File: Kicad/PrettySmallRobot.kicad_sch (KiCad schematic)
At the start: 55 parts, among them J1 TYPE-C-31-M-12, J2 MOTORA_1, J3 MOTORA_2, J4 MOTORB_1, J5 MOTORB_2, J6 BATT+, J7 GND, SW1 SW_Push, SW2 SW_Push, U1 DRV8837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

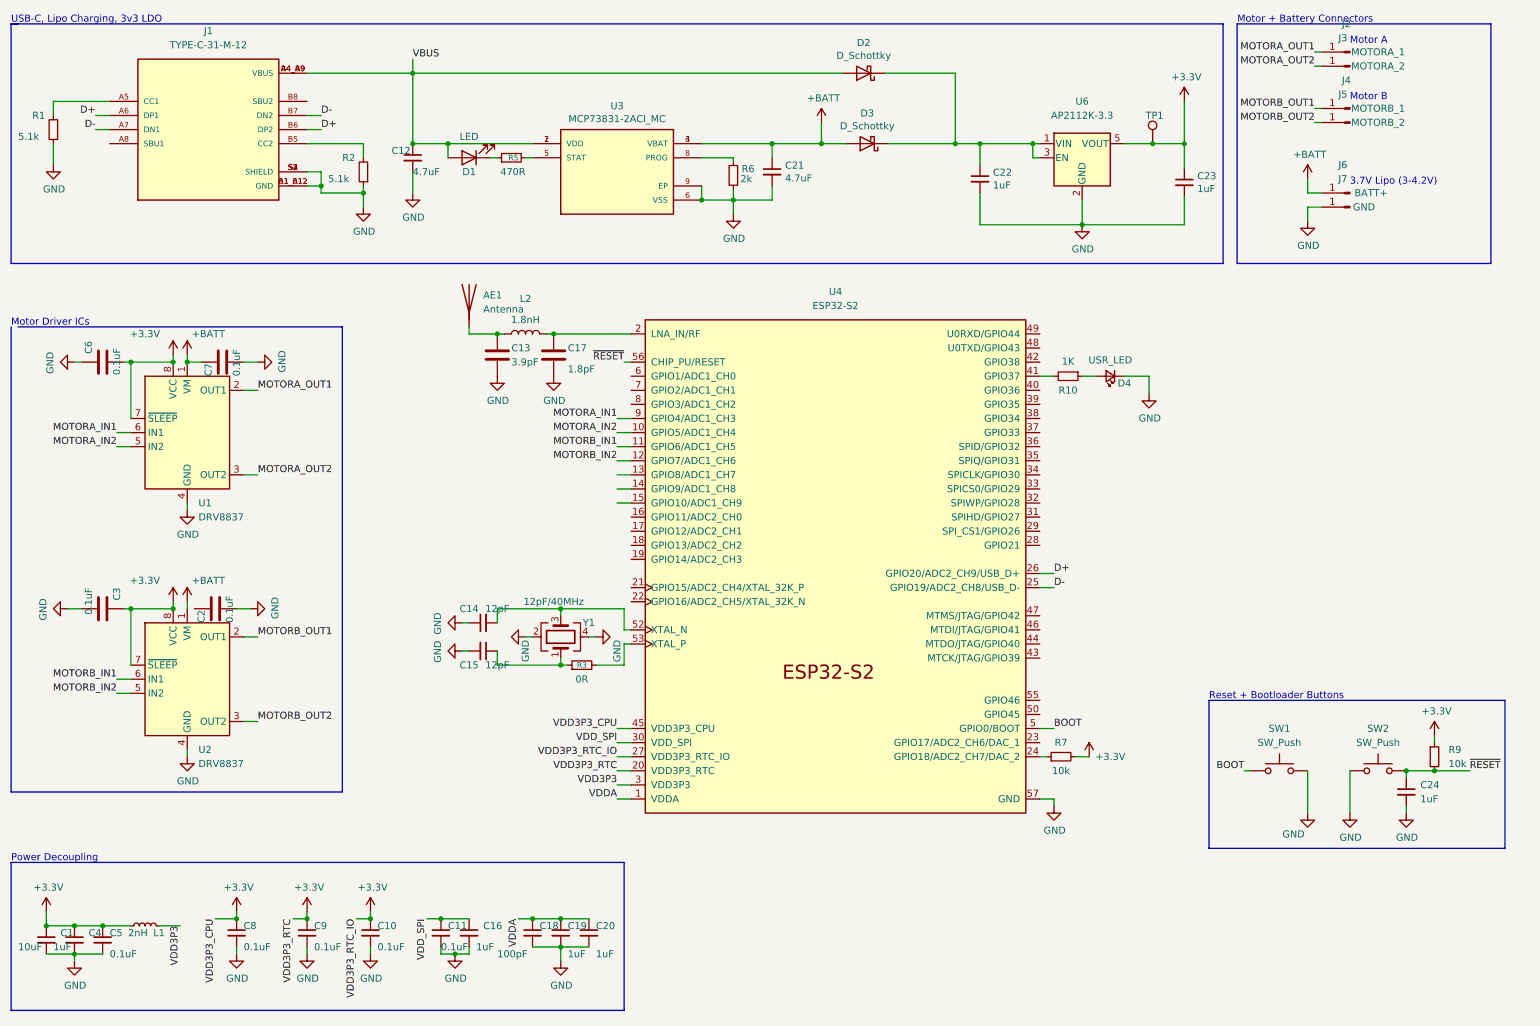
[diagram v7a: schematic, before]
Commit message: fixed drc issues
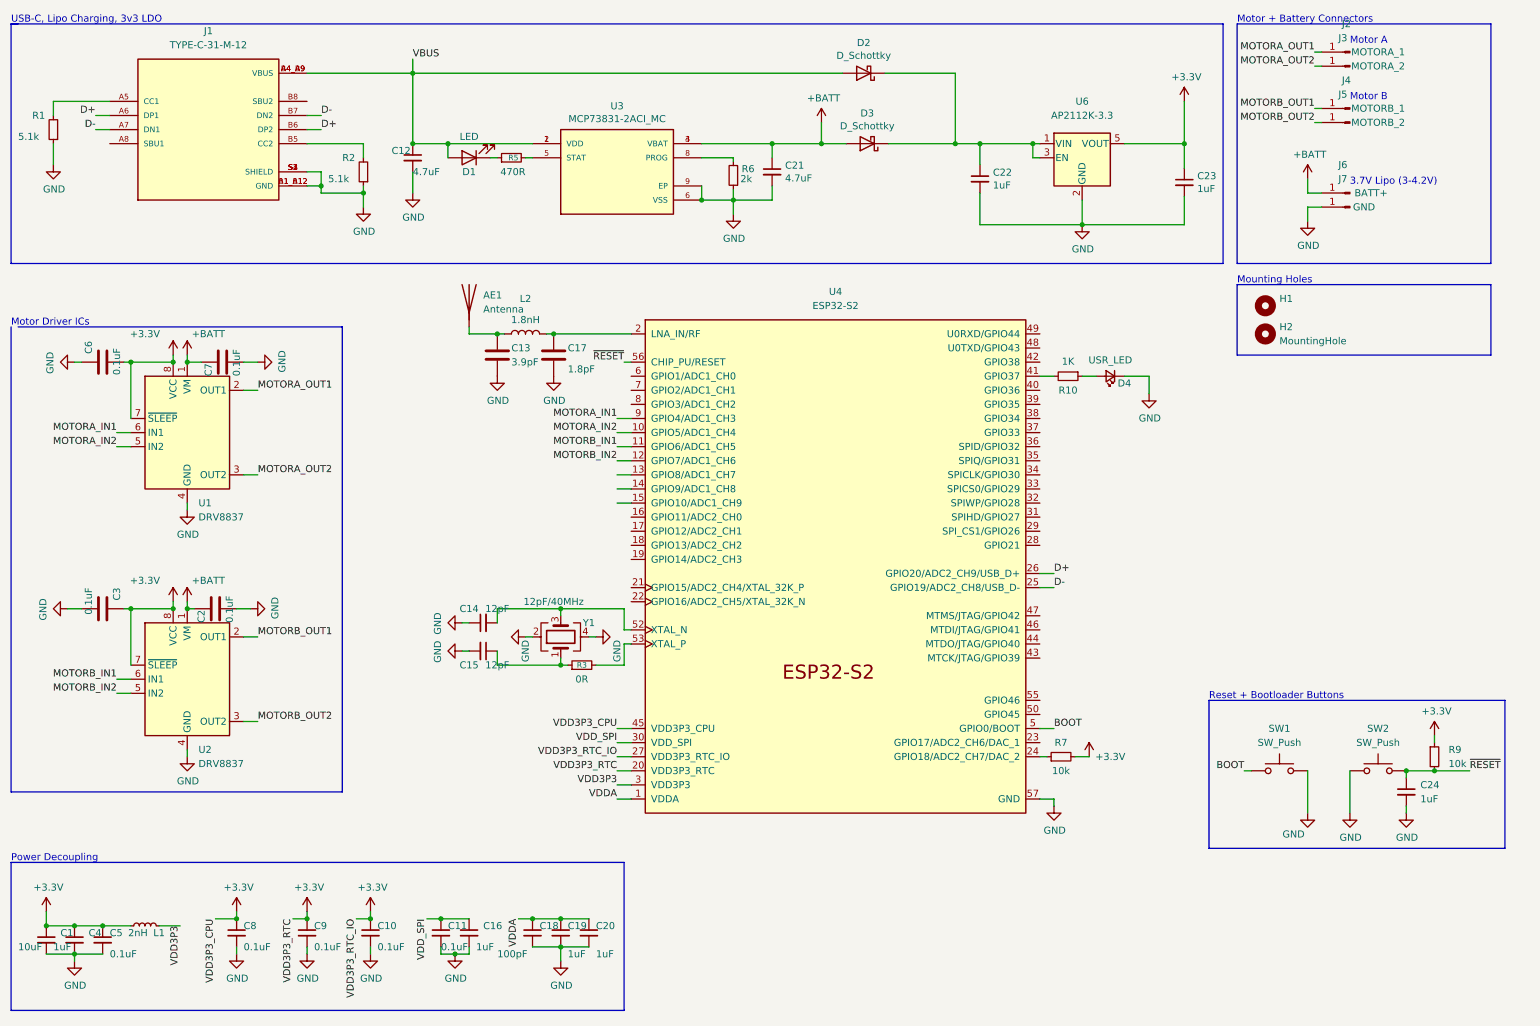
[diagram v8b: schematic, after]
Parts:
- removed TP1: TEST, TestPoint:TestPoint_Plated_Hole_D2.0mm, symbol Connector:TestPoint
- added H1: (no value), symbol Mechanical:MountingHole
- added H2: MountingHole, symbol Mechanical:MountingHole
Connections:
- net +BATT: now also C2.1
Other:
- note added: "Mounting Holes"
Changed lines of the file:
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@@
   (junction (at 91.44 177.8) (diameter 0) (color 0 0 0 0)
   )
-  (junction (at 219.71 38.1) (diameter 0) (color 0 0 0 0)
+  (junction (at 45.72 121.92) (diameter 0) (color 0 0 0 0)
   )
   (junction (at 111.76 72.39) (diameter 0) (color 0 0 0 0)
@@
     (stroke (width 0) (type default) (color 0 0 0 0))
   )
+  (wire (pts (xy 45.72 121.92) (xy 46.99 121.92))
+    (stroke (width 0) (type default) (color 0 0 0 0))
+  )
   (wire (pts (xy 101.6 132.08) (xy 101.6 129.54))
     (stroke (width 0) (type default) (color 0 0 0 0))
@@
     (stroke (width 0) (type default) (color 0 0 0 0))
   )
+  (polyline (pts (xy 280.67 76.2) (xy 234.95 76.2))
+    (stroke (width 0) (type default) (color 0 0 0 0))
+  )
   (wire (pts (xy 77.47 46.99) (xy 77.47 49.53))
     (stroke (width 0) (type default) (color 0 0 0 0))
@@
     (stroke (width 0) (type default) (color 0 0 0 0))
   )
-  (wire (pts (xy 219.71 38.1) (xy 225.425 38.1))
-    (stroke (width 0) (type default) (color 0 0 0 0))
-  )
   (wire (pts (xy 91.44 182.88) (xy 91.44 184.15))
     (stroke (width 0) (type default) (color 0 0 0 0))
@@
     (stroke (width 0) (type default) (color 0 0 0 0))
   )
+  (polyline (pts (xy 234.95 63.5) (xy 234.95 76.2))
+    (stroke (width 0) (type default) (color 0 0 0 0))
+  )
   (wire (pts (xy 101.6 121.92) (xy 113.03 121.92))
     (stroke (width 0) (type default) (color 0 0 0 0))
@@
     (stroke (width 0) (type default) (color 0 0 0 0))
   )
+  (polyline (pts (xy 234.95 63.5) (xy 280.67 63.5))
+    (stroke (width 0) (type default) (color 0 0 0 0))
+  )
   (wire (pts (xy 96.52 71.12) (xy 96.52 72.39))
     (stroke (width 0) (type default) (color 0 0 0 0))
@@
     (stroke (width 0) (type default) (color 0 0 0 0))
   )
-  (wire (pts (xy 214.63 38.1) (xy 219.71 38.1))
+  (wire (pts (xy 214.63 38.1) (xy 225.425 38.1))
     (stroke (width 0) (type default) (color 0 0 0 0))
   )
@@
   )
   (wire (pts (xy 172.085 38.1) (xy 184.15 38.1))
+    (stroke (width 0) (type default) (color 0 0 0 0))
+  )
+  (polyline (pts (xy 280.67 63.5) (xy 280.67 76.2))
     (stroke (width 0) (type default) (color 0 0 0 0))
   )
@@
   )
   (text "Motor + Battery Connectors" (at 234.95 16.51 0)
+    (effects (font (size 1.27 1.27)) (justify left bottom))
+  )
+  (text "Mounting Holes" (at 234.95 63.5 0)
     (effects (font (size 1.27 1.27)) (justify left bottom))
   )
@@
     )
     (pin "1")
+  )
+  (symbol (lib_id "Mechanical:MountingHole") (at 240.03 67.31 0) (unit 1)
+    (in_bom yes) (on_board yes) (fields_autoplaced)
+    (property "Reference" "H1" (id 0) (at 242.57 66.0399 0)
+      (effects (font (size 1.27 1.27)) (justify left))
+    )
+    (property "Value" "" (id 1) (at 242.57 68.5799 0)
+      (effects (font (size 1.27 1.27)) (justify left))
+    )
+    (property "Footprint" "" (id 2) (at 240.03 67.31 0)
+      (effects (font (size 1.27 1.27)) hide)
+    )
+    (property "Datasheet" "~" (id 3) (at 240.03 67.31 0)
+      (effects (font (size 1.27 1.27)) hide)
+    )
   )
   (symbol (lib_id "Device:C_Small") (at 25.4 181.61 0) (unit 1)
@@
     (pin "1")
     (pin "2")
+  )
+  (symbol (lib_id "Mechanical:MountingHole") (at 240.03 72.39 0) (unit 1)
+    (in_bom yes) (on_board yes) (fields_autoplaced)
+    (property "Reference" "H2" (id 0) (at 242.57 71.1199 0)
+      (effects (font (size 1.27 1.27)) (justify left))
+    )
+    (property "Value" "MountingHole" (id 1) (at 242.57 73.6599 0)
+      (effects (font (size 1.27 1.27)) (justify left))
+    )
+    (property "Footprint" "" (id 2) (at 240.03 72.39 0)
+      (effects (font (size 1.27 1.27)) hide)
+    )
+    (property "Datasheet" "~" (id 3) (at 240.03 72.39 0)
+      (effects (font (size 1.27 1.27)) hide)
+    )
   )
   (symbol (lib_id "Device:C") (at 50.8 121.92 90) (unit 1)
@@
     (pin "1")
   )
-  (symbol (lib_id "Connector:TestPoint") (at 219.71 38.1 0) (unit 1)
-    (in_bom yes) (on_board yes)
-    (property "Reference" "TP1" (id 0) (at 218.44 33.02 0)
-      (effects (font (size 1.27 1.27)) (justify left))
-    )
-    (property "Value" "TEST" (id 1) (at 222.25 36.0679 0)
-      (effects (font (size 1.27 1.27)) (justify left) hide)
-    )
-    (property "Footprint" "TestPoint:TestPoint_Plated_Hole_D2.0mm" (id 2) (at 224.79 38.1 0)
-      (effects (font (size 1.27 1.27)) hide)
-    )
-    (property "Datasheet" "~" (id 3) (at 224.79 38.1 0)
-      (effects (font (size 1.27 1.27)) hide)
-    )
-    (pin "1")
-  )
   (symbol (lib_id "power:+3.3V") (at 43.18 76.2 0) (unit 1)
     (in_bom yes) (on_board yes)
@@
       (reference "D4") (unit 1) (value "USR_LED") (footprint "LED_SMD:LED_0402_1005Metric")
     )
+    (path "/0fb5633e-a342-4136-bcf9-1f98010ca419"
+      (reference "H1") (unit 1) (value "MountingHole") (footprint "MountingHole:MountingHole_2.2mm_M2_DIN965_Pad")
+    )
+    (path "/5a7de32a-df6d-4a0f-bbae-de1b96db2496"
+      (reference "H2") (unit 1) (value "MountingHole") (footprint "MountingHole:MountingHole_2.2mm_M2_DIN965_Pad")
+    )
     (path "/3c6b0d4e-fccc-417e-bf34-f237c07621e0"
       (reference "J1") (unit 1) (value "TYPE-C-31-M-12") (footprint "kicad_footprints:HRO_TYPE-C-31-M-12")
@@
       (reference "SW2") (unit 1) (value "SW_Push") (footprint "Button_Switch_SMD:SW_SPST_B3U-1000P")
     )
-    (path "/ca86f163-4450-470c-84f8-af0fe0b9e144"
-      (reference "TP1") (unit 1) (value "TEST") (footprint "TestPoint:TestPoint_Plated_Hole_D2.0mm")
-    )
     (path "/7abf7546-ee90-4e42-adf8-adf0bc998f8a"
